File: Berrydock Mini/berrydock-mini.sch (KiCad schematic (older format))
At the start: 0 parts

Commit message: added circuit for ATC4088
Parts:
- added C?: 10uF, symbol C_Small
- added CON?: BARREL_JACK, symbol BARREL_JACK
- added D?: D_Schottky_Small, symbol D_Schottky_Small
- added J?: RJ45, symbol RJ45
- added L?: INDUCTOR_SMALL, symbol INDUCTOR_SMALL
- added R?: R_Small, symbol R_Small
- added U?: Omega2, symbol Omega2
- added U?: ACT4088, symbol ACT4088
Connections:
- net labels added: +5V, GND, VDD
- wire segments 0 -> 5
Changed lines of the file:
@@
 LIBS:valves
 LIBS:berrydock-components
+LIBS:berrydock-mini-cache
 EELAYER 25 0
 EELAYER END
@@
 Comment4 ""
 $EndDescr
+$Comp
+L Omega2 U?
+U 1 1 57E7AC5B
+P 4900 4100
+F 0 "U?" H 5150 4650 60  0000 C CNN
+F 1 "Omega2" H 4750 4650 60  0000 C CNN
+F 2 "" H 4900 4100 60  0001 C CNN
+F 3 "" H 4900 4100 60  0001 C CNN
+	1    4900 4100
+	1    0    0    -1
+$EndComp
+$Comp
+L RJ45 J?
+U 1 1 57E7E2BB
+P 8850 2250
+F 0 "J?" H 9050 2750 50  0000 C CNN
+F 1 "RJ45" H 8700 2750 50  0000 C CNN
+F 2 "" H 8850 2250 50  0000 C CNN
+F 3 "" H 8850 2250 50  0000 C CNN
+	1    8850 2250
+	1    0    0    -1
+$EndComp
+$Comp
+L C_Small C?
+U 1 1 57E7EA54
+P 5550 1550
+F 0 "C?" H 5560 1620 50  0000 L CNN
+F 1 "10uF" H 5560 1470 50  0000 L CNN
+F 2 "" H 5550 1550 50  0000 C CNN
+F 3 "" H 5550 1550 50  0000 C CNN
+	1    5550 1550
+	-1   0    0    -1
+$EndComp
+$Comp
+L R_Small R?
+U 1 1 57E7EA81
+P 4700 2500
+F 0 "R?" H 4730 2520 50  0000 L CNN
+F 1 "R_Small" H 4730 2460 50  0000 L CNN
+F 2 "" H 4700 2500 50  0000 C CNN
+F 3 "" H 4700 2500 50  0000 C CNN
+	1    4700 2500
+	1    0    0    -1
+$EndComp
+$Comp
+L D_Schottky_Small D?
+U 1 1 57E7EAA0
+P 5250 2500
+F 0 "D?" H 5200 2580 50  0000 L CNN
+F 1 "D_Schottky_Small" H 4970 2420 50  0000 L CNN
+F 2 "" V 5250 2500 50  0000 C CNN
+F 3 "" V 5250 2500 50  0000 C CNN
+	1    5250 2500
+	1    0    0    -1
+$EndComp
+$Comp
+L INDUCTOR_SMALL L?
+U 1 1 57E7EAC1
+P 4950 1450
+F 0 "L?" H 4950 1550 50  0000 C CNN
+F 1 "INDUCTOR_SMALL" H 4950 1400 50  0000 C CNN
+F 2 "" H 4950 1450 50  0000 C CNN
+F 3 "" H 4950 1450 50  0000 C CNN
+	1    4950 1450
+	1    0    0    -1
+$EndComp
+$Comp
+L ACT4088 U?
+U 1 1 57E7EEEA
+P 6050 1650
+F 0 "U?" H 6250 2050 60  0000 C CNN
+F 1 "ACT4088" H 5900 2050 60  0000 C CNN
+F 2 "" H 6150 1600 60  0001 C CNN
+F 3 "" H 6150 1600 60  0001 C CNN
+	1    6050 1650
+	1    0    0    -1
+$EndComp
+$Comp
+L GND #PWR?
+U 1 1 57E7F0D9
+P 4800 1950
+F 0 "#PWR?" H 4800 1700 50  0001 C CNN
+F 1 "GND" H 4800 1800 50  0000 C CNN
+F 2 "" H 4800 1950 50  0000 C CNN
+F 3 "" H 4800 1950 50  0000 C CNN
+	1    4800 1950
+	1    0    0    -1
+$EndComp
+$Comp
+L +5V #PWR?
+U 1 1 57E7F0FB
+P 6400 950
+F 0 "#PWR?" H 6400 800 50  0001 C CNN
+F 1 "+5V" H 6400 1090 50  0000 C CNN
+F 2 "" H 6400 950 50  0000 C CNN
+F 3 "" H 6400 950 50  0000 C CNN
+	1    6400 950
+	1    0    0    -1
+$EndComp
+$Comp
+L BARREL_JACK CON?
+U 1 1 57E7F175
+P 1900 2050
+F 0 "CON?" H 1900 2300 50  0000 C CNN
+F 1 "BARREL_JACK" H 1900 1850 50  0000 C CNN
+F 2 "" H 1900 2050 50  0000 C CNN
+F 3 "" H 1900 2050 50  0000 C CNN
+	1    1900 2050
+	1    0    0    -1
+$EndComp
+$Comp
+L GND #PWR?
+U 1 1 57E7F368
+P 2300 2250
+F 0 "#PWR?" H 2300 2000 50  0001 C CNN
+F 1 "GND" H 2300 2100 50  0000 C CNN
+F 2 "" H 2300 2250 50  0000 C CNN
+F 3 "" H 2300 2250 50  0000 C CNN
+	1    2300 2250
+	1    0    0    -1
+$EndComp
+Wire Wire Line
+	2300 2050 2300 2250
+Wire Wire Line
+	2300 2150 2200 2150
+$Comp
+L VDD #PWR?
+U 1 1 57E7F5C7
+P 2300 1850
+F 0 "#PWR?" H 2300 1700 50  0001 C CNN
+F 1 "VDD" H 2300 2000 50  0000 C CNN
+F 2 "" H 2300 1850 50  0000 C CNN
+F 3 "" H 2300 1850 50  0000 C CNN
+	1    2300 1850
+	1    0    0    -1
+$EndComp
+Wire Wire Line
+	2300 1850 2300 1950
+Wire Wire Line
+	2300 1950 2200 1950
+Wire Wire Line
+	2200 2050 2300 2050
+Connection ~ 2300 2150
 $EndSCHEMATC

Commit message: Added First part of power Circuit, added lipo protection circuit
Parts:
- removed CON?: BARREL_JACK, symbol BARREL_JACK
- added C?: 22nF, symbol C_Small
- added C?: 4.7uF, symbol C_Small
- added C?: 10uF, symbol C_Small
- added C?: 22uF, symbol C_Small
- added C?: 100nF, symbol C_Small
- added P?: CONN_01X04, symbol CONN_01X04
- added P?: CONN_01X02, symbol CONN_01X02
- added R?: 26.1K, symbol R_Small
- added R?: 150K, symbol R_Small
- added R?: 28.7K, symbol R_Small
- added R?: 100R, symbol R_Small
- added R?: 1K, symbol R_Small
- added U?: AMS1117, symbol AMS1117
- added U?: DW01-P, symbol DW01-P
- added U?: FS8205A, symbol FS8205A
- D?: value D_Schottky_Small -> B240A
- L?: value INDUCTOR_SMALL -> 4.7uH
- R?: value R_Small -> 100K
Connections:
- net labels added: +3.3V, +3.3VP, +5P, +5VD, +5VP, BAT_-, OC, OD, VPP
- wire segments 5 -> 67
- no-connect marks 0 -> 3
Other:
- note added: "3.3V LDO (maybe get something better)"
- note added: "5V Regulator"
- note added: "LiPo JST"
- note added: "LiPo Protection Circuit"
- note added: "Select 5V Source:\nEXT or USB or LIPO\nmake it like a triangle\non PCB"
- moved on the sheet: C?, D?, J?, L?, R?

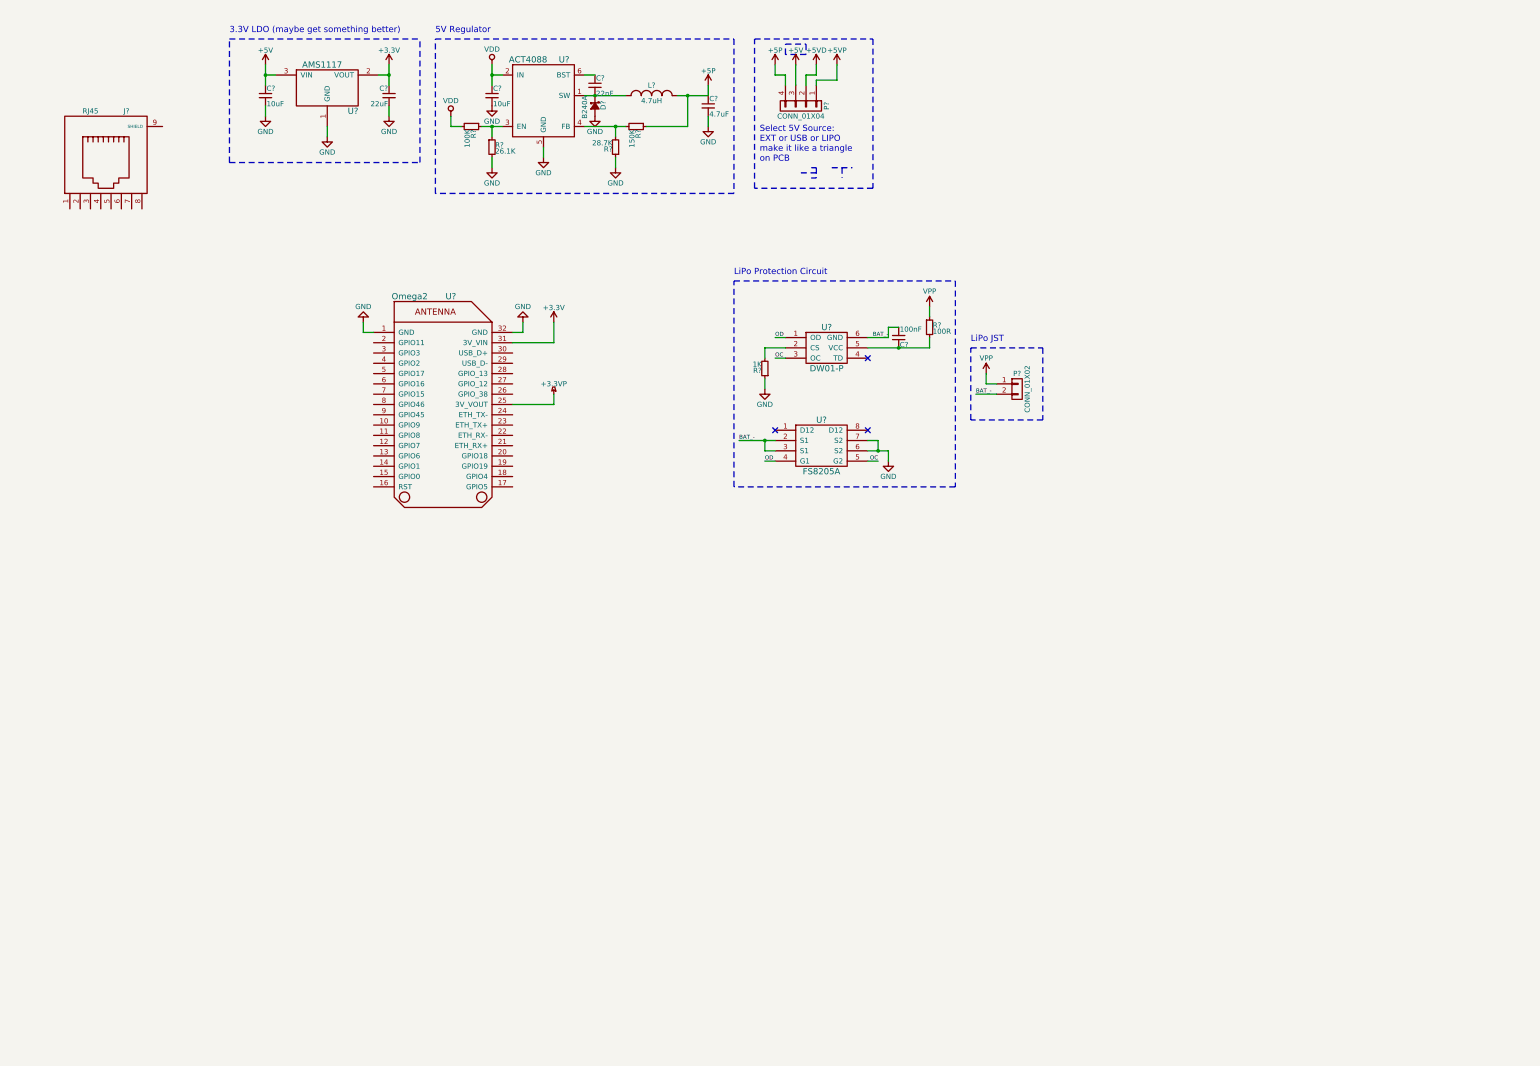
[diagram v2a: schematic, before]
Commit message: 75% of schematic finished, power stuff all finished up.
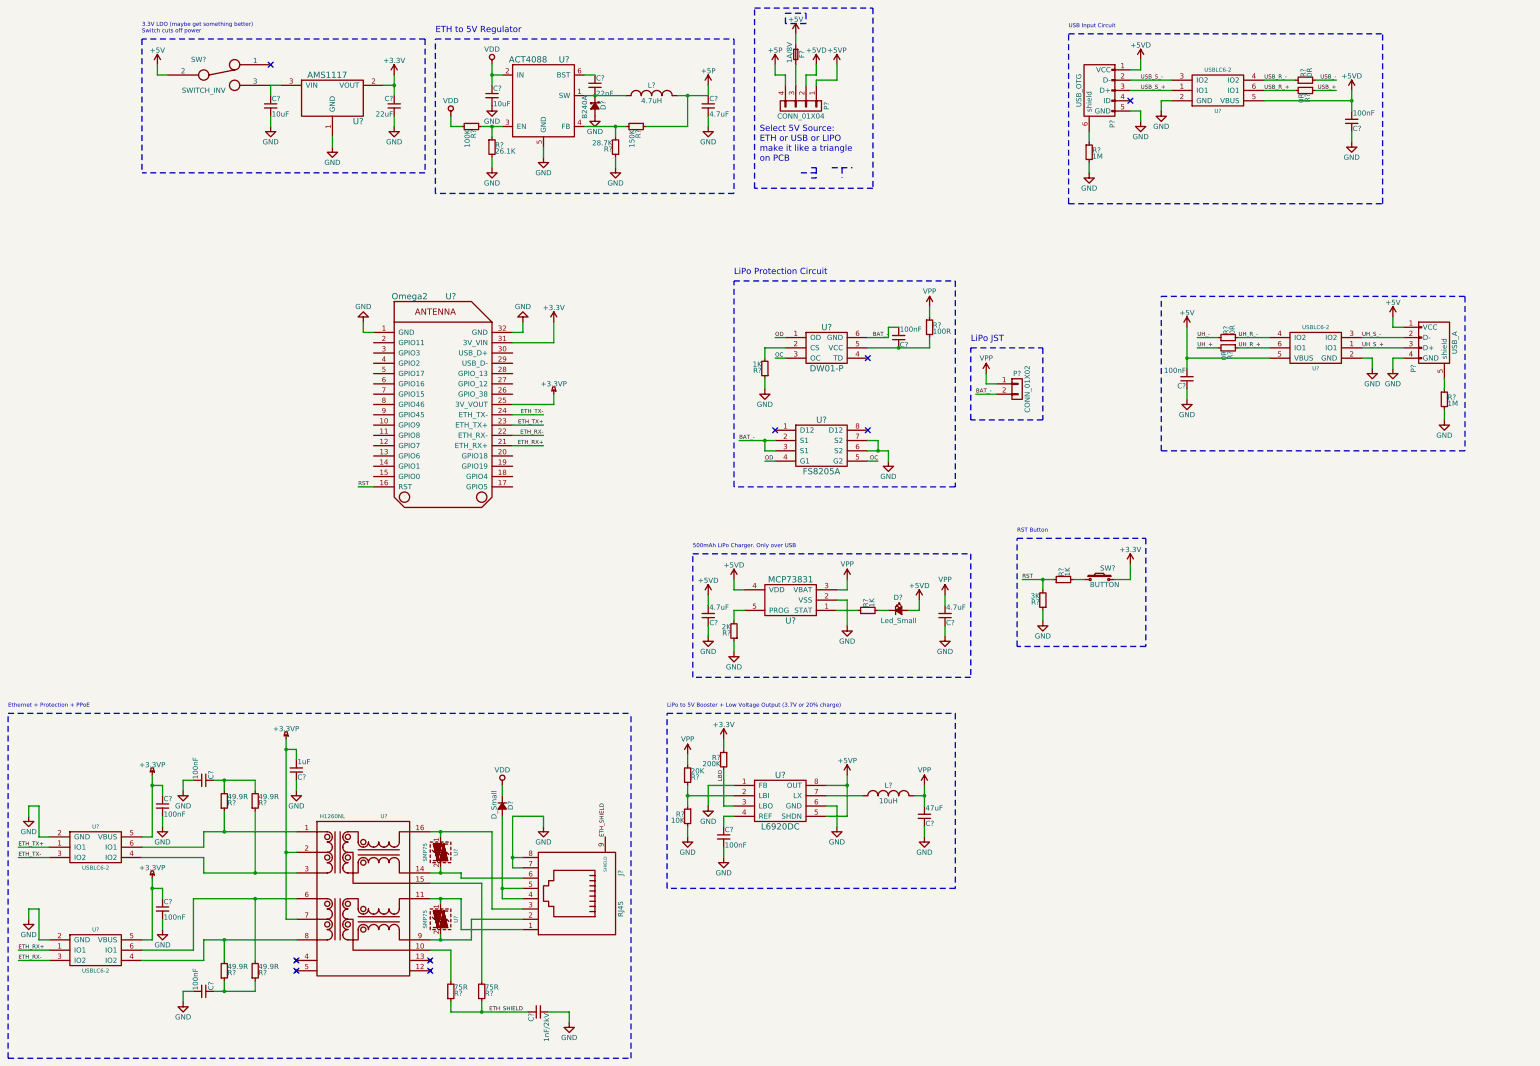
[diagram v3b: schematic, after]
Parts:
- added C? (x2): 4.7uF, symbol C_Small
- added C? (x7): 100nF, symbol C_Small
- added C?: 47uF, symbol C_Small
- added C?: 1uF, symbol C_Small
- added C?: 1nF/2kV, symbol C_Small
- added D?: Led_Small, symbol Led_Small
- added D?: D_Small, symbol D_Small
- added F?: 1A/8V, symbol F_Small
- added L?: 10uH, symbol INDUCTOR_SMALL
- added P?: USB_OTG, symbol USB_OTG
- added P?: USB_A, symbol USB_A
- added R?: 2K, symbol R_Small
- added R? (x2): 1K, symbol R_Small
- added R?: 20K, symbol R_Small
- added R?: 10K, symbol R_Small
- added R?: 200K, symbol R_Small
- added R? (x2): 1M, symbol R_Small
- added R?: 3K, symbol R_Small
- added R? (x4): 49.9R, symbol R_Small
- added R? (x2): 75R, symbol R_Small
- added R? (x4): 0R, symbol R_Small
- added SW?: SWITCH_INV, symbol SWITCH_INV
- added SW?: BUTTON, symbol SW_PUSH_SMALL_H
- added U?: MCP73831, symbol MCP73831
- added U?: L6920DC, symbol L6920DC
- added U? (x4): USBLC6-2, symbol USBLC6-2
- added U?: H1260NL, symbol H1260NL
- added U? (x2): SMP75, symbol SMP75
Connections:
- net +3.3VP: now also C?.1, C?.1, C?.2, U?.2, U?.5 (VBUS), U?.5 (VBUS), U?.7
- net +3V3: now also R?.1, SW?.2
- net +5V: now also C?.2, F?.1, P?.1 (VCC), SW?.2, U?.5 (VBUS); no longer C?.1, P?.3 (P3), U?.3 (VIN)
- net +5VD: now also C?.2, C?.2, D?.2 (A), P?.1 (VCC), U?.4 (VDD), U?.5 (VBUS)
- net +5VP: now also U?.5 (SHDN), U?.8 (OUT)
- net GND: now also J?.7, J?.8, C?.1, C?.1, C?.1, C?.1, C?.1, C?.1, C?.2, C?.2, C?.2, C?.2, C?.2, C?.2, P?.4 (GND), P?.5 (GND), R?.1, R?.1, R?.2, R?.2, R?.2, U?.1 (FB), U?.2 (GND), U?.2 (GND), U?.2 (GND), U?.2 (GND), U?.2 (VSS), U?.6 (GND)
- net VDD: now also D?.1 (K)
- net VPP: now also C?.2, C?.2, L?.2, R?.2, U?.3 (VBAT)
- net RST: now reaches U?.16 (RST)
- net RST: now also R?.1, R?.2
- net ETH_RX+: now reaches U?.21 (ETH_RX+)
- net ETH_RX+: now also U?.1 (IO1)
- net ETH_RX-: now reaches U?.22 (ETH_RX-)
- net ETH_RX-: now also U?.3 (IO2)
- net ETH_TX+: now reaches U?.23 (ETH_TX+)
- net ETH_TX+: now also U?.1 (IO1)
- net ETH_TX-: now reaches U?.24 (ETH_TX-)
- net ETH_TX-: now also U?.3 (IO2)
- net at J?.1: now also U?.1, U?.11
- net at J?.2: now also U?.2, U?.9
- net at J?.3: now also U?.1, U?.16
- net at J?.4: now also J?.5, D?.2 (A)
- net at J?.6: now also U?.14, U?.2
- net ETH_SHIELD: now reaches J?.9 (SHIELD)
- net ETH_SHIELD: now also C?.1, R?.1, R?.1
- new net: C?.1, SW?.3, U?.3 (VIN)
- new net: F?.2, P?.3 (P3)
- new net: R?.1, U?.1 (STAT)
- new net: R?.2, U?.5 (PROG)
- new net: D?.1 (K), R?.2
- new net: R?.1, R?.1, U?.2 (LBI)
- new net: C?.1, U?.4 (REF)
- new net: L?.1, U?.7 (LX)
- new net: P?.6 (shield), R?.1
- new net: R?.2, SW?.1
- new net: R?.1, U?.1, U?.6 (IO1)
- new net: R?.2, U?.10
- new net: R?.2, U?.15
- new net: R?.1, U?.3, U?.4 (IO2)
- new net: R?.2, U?.6, U?.6 (IO1)
- new net: R?.2, U?.4 (IO2), U?.8
- new net: C?.1, R?.2, R?.2
- new net: C?.1, R?.1, R?.1
- new net: P?.5 (shield), R?.1
- new net LBO: R?.2, U?.3 (LBO)
- new net UH_+: R?.2
- new net UH_-: R?.1
- new net UH_R_+: R?.1, U?.6 (IO1)
- new net UH_R_-: R?.2, U?.4 (IO2)
- new net UH_S_+: P?.3 (D+), U?.1 (IO1)
- new net UH_S_-: P?.2 (D-), U?.3 (IO2)
- new net USB_+: R?.1
- new net USB_-: R?.2
- new net USB_R_+: R?.2, U?.6 (IO1)
- new net USB_R_-: R?.1, U?.4 (IO2)
- new net USB_S_+: P?.3 (D+), U?.1 (IO1)
- new net USB_S_-: P?.2 (D-), U?.3 (IO2)
- no-connect marks 3 -> 9
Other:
- note added: "3.3V LDO (maybe get something better)\nSwitch cuts off power"
- note added: "500mAh LiPo Charger. Only over USB"
- note added: "ETH to 5V Regulator"
- note added: "Ethernet + Protection + PPoE"
- note added: "LiPo to 5V Booster + Low Voltage Output (3.7V or 20% charge)"
- note added: "RST Button"
- note added: "Select 5V Source:\nETH or USB or LIPO\nmake it like a triangle\non PCB"
- note added: "USB Input Circuit"
- note removed: "3.3V LDO (maybe get something better)"
- note removed: "5V Regulator"
- note removed: "Select 5V Source:\nEXT or USB or LIPO\nmake it like a triangle\non PCB"
- moved on the sheet: C?, J?, U?

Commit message: Added CP2102 USB Serial
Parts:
- added C?: 100nF, symbol C_Small
- added C? (x2): 1uF, symbol C_Small
- added P? (x2): CONN_01X16, symbol CONN_01X16
- added R? (x2): 3K, symbol R_Small
- added R? (x2): 1K, symbol R_Small
- added U?: CP2102, symbol CP2102
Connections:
- net +3.3VP: now also P?.9 (P9)
- net +3V3: now also P?.15 (P15)
- net +5V: now also C?.2, U?.7 (REGIN), U?.9 (~RST)
- net +5VD: now also C?.2, U?.8 (VBUS)
- net ETH_RX+: now also P?.5 (P5)
- net ETH_RX-: now also P?.6 (P6)
- net ETH_TX+: now also P?.7 (P7)
- net ETH_TX-: now also P?.8 (P8)
- net GND: now also C?.1, C?.1, C?.2, P?.1 (P1), P?.16 (P16), R?.1, R?.2, U?.29 (GND2), U?.3 (GND), U?.30 (GND3)
- net RST: now also P?.16 (P16); no longer R?.1, R?.2
- net UH_+: now also U?.30 (USB_D+), P?.14 (P14)
- net UH_-: now also U?.29 (USB_D-), P?.13 (P13)
- net USB_+: now also U?.4 (D+)
- net USB_-: now also U?.5 (D-)
- net GPIO9: now reaches U?.10 (GPIO9)
- net GPIO9: now also P?.10 (P10)
- net GPIO8: now reaches U?.11 (GPIO8)
- net GPIO8: now also P?.11 (P11)
- net GPIO7: now reaches U?.12 (GPIO7)
- net GPIO7: now also P?.12 (P12)
- net GPIO6: now reaches U?.13 (GPIO6)
- net GPIO6: now also P?.13 (P13)
- net GPIO1: now reaches U?.14 (GPIO1)
- net GPIO1: now also P?.14 (P14)
- net GPIO0: now reaches U?.15 (GPIO0)
- net GPIO0: now also P?.15 (P15)
- net GPIO5: now reaches U?.17 (GPIO5)
- net GPIO5: now also P?.1 (P1)
- net GPIO4: now reaches U?.18 (GPIO4)
- net GPIO4: now also P?.2 (P2)
- net GPIO19: now reaches U?.19 (GPIO19)
- net GPIO19: now also P?.3 (P3)
- net GPIO11: now reaches U?.2 (GPIO11)
- net GPIO11: now also P?.2 (P2)
- net GPIO18: now reaches U?.20 (GPIO18)
- net GPIO18: now also P?.4 (P4)
- net FW_RST: now reaches U?.26 (GPIO_38)
- net FW_RST: now also R?.1, R?.2, P?.10 (P10)
- net TX0: now reaches U?.27 (GPIO_12)
- net TX0: now also P?.11 (P11), R?.1, R?.2
- net RX0: now reaches U?.28 (GPIO_13)
- net RX0: now also P?.12 (P12), R?.1, R?.2
- net GPIO3: now reaches U?.3 (GPIO3)
- net GPIO3: now also P?.3 (P3)
- net GPIO2: now reaches U?.4 (GPIO2)
- net GPIO2: now also P?.4 (P4)
- net GPIO17: now reaches U?.5 (GPIO17)
- net GPIO17: now also P?.5 (P5)
- net GPIO16: now reaches U?.6 (GPIO16)
- net GPIO16: now also P?.6 (P6)
- net GPIO15: now reaches U?.7 (GPIO15)
- net GPIO15: now also P?.7 (P7)
- net GPIO46: now reaches U?.8 (GPIO46)
- net GPIO46: now also P?.8 (P8)
- net GPIO45: now reaches U?.9 (GPIO45)
- net GPIO45: now also P?.9 (P9)
- new net: C?.1, U?.6 (VDD)
- new net U_RX: R?.2, U?.25 (RXD)
- new net U_TX: R?.1, U?.26 (TXD)
- no-connect marks 9 -> 17
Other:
- note added: "Direct Pinout"
- note added: "USB Host"
- note added: "USB Serial"

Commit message: Added power flags and fixed problems for ERC
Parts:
- removed U?: CP2102, symbol CP2102
- added R21: 10K, symbol R_Small
- added U15: CP2102, symbol CP2102
- gave numbers to parts that had none: 79
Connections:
- net +5V: now also R21.1, U15.7 (REGIN)
- net +5VD: now also U15.8 (VBUS)
- net GND: now also U15.29 (GND2), U15.3 (GND), U15.30 (GND3)
- net USB_+: now also U15.4 (D+)
- net USB_-: now also U15.5 (D-)
- net U_RX: now also U15.25 (RXD)
- net U_TX: now also U15.26 (TXD)
- net SW: now reaches C5.1, SW1.3, U3.3 (VIN)
- net at C19.1: now also U15.6 (VDD)
- new net: R21.2, U15.9 (~RST)
- no-connect marks 17 -> 13

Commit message: Added ADC
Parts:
- removed P1, P2: CONN_01X16, symbol CONN_01X16
- added C17: 10uF, symbol C_Small
- added C18: 100nF, symbol C_Small
- added F2, F3: FERRITE_BEAD, symbol FERRITE_BEAD
- added P1, P2: CONN_01X18, symbol CONN_01X18
- added R21, R22: 10K, symbol R_Small
- added R26, R29: 4K7, symbol R_Small
- added U14: ADS1015, symbol ADS1015
- renumbered C17 to C19, C18 to C20, C19 to C21, C20 to C22, C21 to C23, R21 to R23, R22 to R24, R23 to R25, R24 to R27, R25 to R28, R26 to R30, R27 to R31, R28 to R32, R29 to R33, R30 to R34, U14 to U15, U15 to U16
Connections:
- net +3.3VP: now also P2.8 (P8)
- net +3V3: now also C17.2, F2.2, P2.2 (P2)
- net ETH_RX+: now also P2.12 (P12)
- net ETH_RX-: now also P2.11 (P11)
- net ETH_TX+: now also P2.10 (P10)
- net ETH_TX-: now also P2.9 (P9)
- net FW_RST: now also P2.7 (P7)
- net GND: now also C17.1, F3.1, P1.1 (P1), P2.1 (P1)
- net GPIO0: now also P1.15 (P15)
- net GPIO1: now also P1.14 (P14)
- net GPIO11: now also P1.2 (P2)
- net GPIO15: now also P1.7 (P7)
- net GPIO16: now also P1.6 (P6)
- net GPIO17: now also P1.5 (P5)
- net GPIO18: now also P2.13 (P13)
- net GPIO19: now also P2.14 (P14)
- net GPIO2: now also P1.4 (P4)
- net GPIO3: now also P1.3 (P3)
- net GPIO4: now also P2.15 (P15), R26.1, U14.10 (SCL)
- net GPIO45: now also P1.9 (P9)
- net GPIO46: now also P1.8 (P8)
- net GPIO5: now also P2.16 (P16), R29.2, U14.9 (SDA)
- net GPIO6: now also P1.13 (P13)
- net GPIO7: now also P1.12 (P12)
- net GPIO8: now also P1.11 (P11)
- net GPIO9: now also P1.10 (P10)
- net RST: now also P1.16 (P16)
- net RX0: now also P2.5 (P5)
- net TX0: now also P2.6 (P6)
- net UH_+: now also P2.3 (P3)
- net UH_-: now also P2.4 (P4)
- new net: R22.1, U14.1 (ADDR)
- new net: R21.1, U14.2 (ALERT/RDY)
- new net +3.3VADC: C18.2, F2.1, R21.2, R26.2, R29.1, U14.8 (VDD)
- new net AIN0: P1.17 (P17), U14.4 (AIN0)
- new net AIN1: P2.17 (P17), U14.5 (AIN1)
- new net AIN2: P1.18 (P18), U14.6 (AIN2)
- new net AIN3: P2.18 (P18), U14.7 (AIN3)
- new net GNDA: C18.1, F3.2, R22.2, U14.3 (GND)
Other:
- note added: "ADC"
- note added: "Power Flags"
- moved on the sheet: C19, C21, R23, R31, R32, R33, R34, U16
